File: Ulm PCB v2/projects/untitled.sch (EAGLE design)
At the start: 26 parts, among them U1 FT232RLSSOP, U2 MCP73831, U3 SPX3819-3.3, X2 USB-SMD-NS

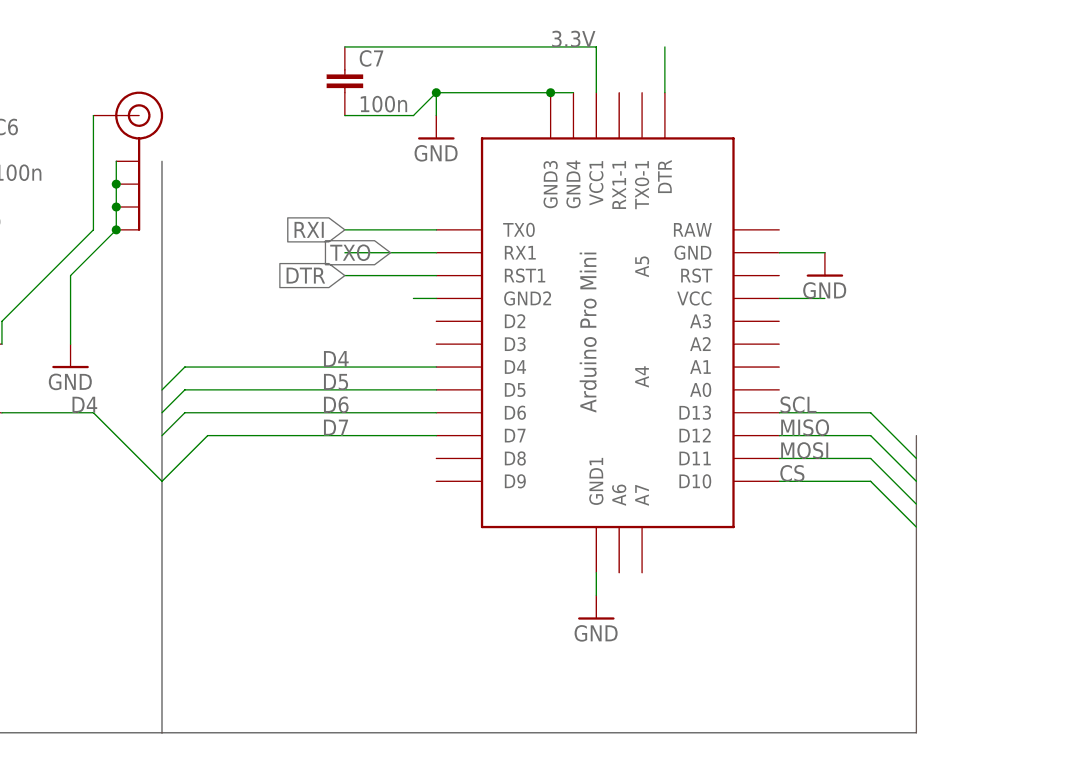
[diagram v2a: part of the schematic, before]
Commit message: nicing of some traces
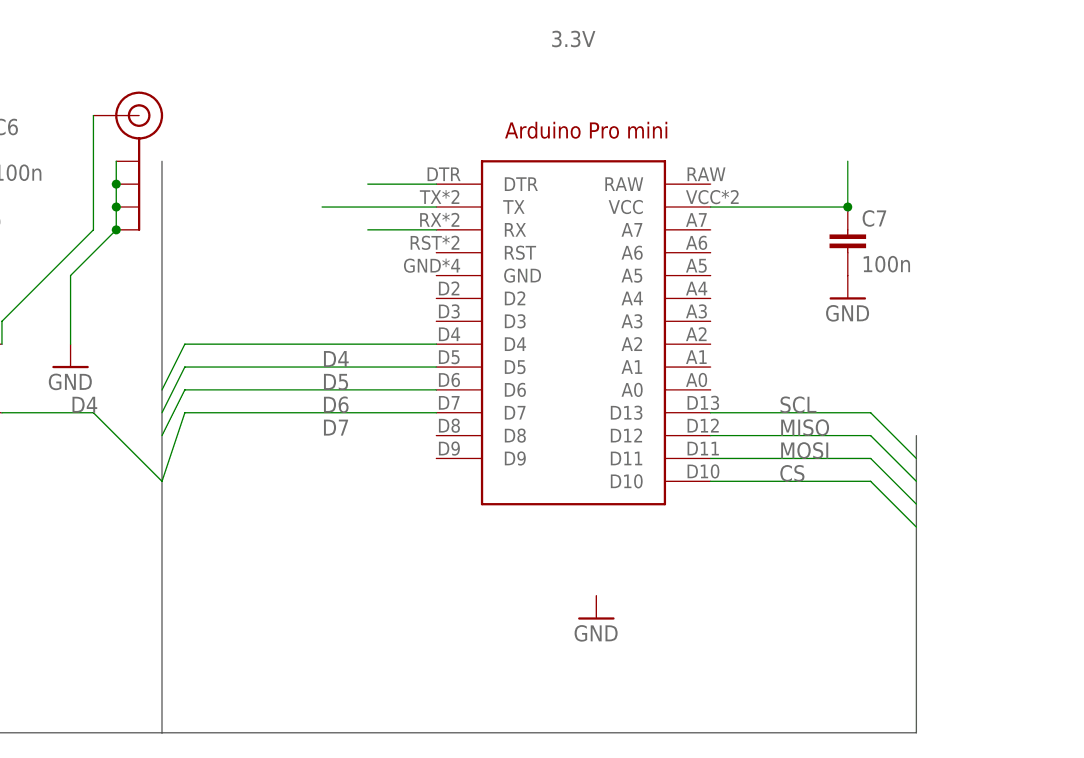
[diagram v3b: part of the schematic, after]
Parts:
- U$1: value ABK-PRO-MINI -> (none); device Arduino-clone:ABK-PRO-MINI -> arduinopromini:ARDUINO_PRO_MINI
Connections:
- removed net N$9: U$1.DTR
- net 3.3V: no longer U$1.VCC1
- net DTR: now also U$1.DTR; no longer U$1.RST1
- net GND: no longer U$1.GND, U$1.GND1, U$1.GND2, U$1.GND3, U$1.GND4
- net RXI: now also U$1.TX; no longer U$1.TX0
- net TXO: now also U$1.RX; no longer U$1.RX1
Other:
- moved on the sheet: C7
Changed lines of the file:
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@@
 </classes>
 <parts>
-<part name="U$1" library="Arduino-clone" deviceset="ABK-PRO-MINI" device=""/>
+<part name="U$1" library="arduinopromini" deviceset="ARDUINO_PRO_MINI" device=""/>
 <part name="GND4" library="supply1" deviceset="GND" device=""/>
 <part name="GND6" library="supply1" deviceset="GND" device=""/>
@@
 <part name="U$3" library="SparkFun" deviceset="5V" device=""/>
 <part name="U$4" library="SparkFun" deviceset="5V" device="" value="3.3V"/>
-<part name="GND1" library="supply1" deviceset="GND" device=""/>
 <part name="U2" library="SparkFun-PowerIC" deviceset="MCP73831" device=""/>
 <part name="R3" library="rcl" library_urn="urn:adsk.eagle:library:334" deviceset="R-EU_" device="R0603" value="330"/>
@@
 </plain>
 <instances>
-<instance part="U$1" gate="G$1" x="177.8" y="401.32"/>
-<instance part="GND4" gate="1" x="154.94" y="424.18"/>
+<instance part="U$1" gate="G$1" x="170.18" y="403.86"/>
+<instance part="GND4" gate="1" x="200.66" y="406.4"/>
 <instance part="GND6" gate="1" x="172.72" y="370.84"/>
 <instance part="C2" gate="G$1" x="-142.24" y="215.9"/>
@@
 <instance part="U$3" gate="G$1" x="-114.3" y="238.76"/>
 <instance part="U$4" gate="G$1" x="-43.18" y="233.68"/>
-<instance part="GND1" gate="1" x="198.12" y="408.94"/>
 <instance part="U2" gate="G$1" x="-86.36" y="307.34"/>
 <instance part="R3" gate="G$1" x="-106.68" y="299.72"/>
@@
 <instance part="P+3" gate="VCC" x="104.14" y="434.34"/>
 <instance part="C6" gate="G$1" x="104.14" y="424.18"/>
-<instance part="C7" gate="G$1" x="144.78" y="431.8"/>
+<instance part="C7" gate="G$1" x="200.66" y="414.02"/>
 <instance part="U$6" gate="G$1" x="93.98" y="401.32"/>
 <instance part="GND15" gate="1" x="104.14" y="416.56"/>
@@
 <net name="GND" class="0">
 <segment>
-<pinref part="U$1" gate="G$1" pin="GND4"/>
-<pinref part="U$1" gate="G$1" pin="GND3"/>
-<wire x1="170.18" y1="429.26" x2="167.64" y2="429.26" width="0.1524" layer="91"/>
-<wire x1="167.64" y1="429.26" x2="154.94" y2="429.26" width="0.1524" layer="91"/>
-<wire x1="154.94" y1="429.26" x2="154.94" y2="426.72" width="0.1524" layer="91"/>
-<junction x="167.64" y="429.26"/>
 <pinref part="GND4" gate="1" pin="GND"/>
 <pinref part="C7" gate="G$1" pin="2"/>
-<wire x1="144.78" y1="426.72" x2="152.4" y2="426.72" width="0.1524" layer="91"/>
-<wire x1="152.4" y1="426.72" x2="154.94" y2="429.26" width="0.1524" layer="91"/>
-<junction x="154.94" y="429.26"/>
-</segment>
-<segment>
-<pinref part="U$1" gate="G$1" pin="GND1"/>
-<wire x1="172.72" y1="375.92" x2="172.72" y2="373.38" width="0.1524" layer="91"/>
-<pinref part="GND6" gate="1" pin="GND"/>
-</segment>
-<segment>
-<pinref part="U$1" gate="G$1" pin="GND2"/>
-<wire x1="154.94" y1="406.4" x2="152.4" y2="406.4" width="0.1524" layer="91"/>
 </segment>
 <segment>
@@
 </segment>
 <segment>
-<pinref part="U$1" gate="G$1" pin="GND"/>
-<wire x1="193.04" y1="411.48" x2="198.12" y2="411.48" width="0.1524" layer="91"/>
-<pinref part="GND1" gate="1" pin="GND"/>
-</segment>
-<segment>
 <wire x1="-33.02" y1="279.4" x2="-33.02" y2="297.18" width="0.1524" layer="91"/>
 <pinref part="GND12" gate="1" pin="GND"/>
@@
 </segment>
 </net>
-<net name="N$9" class="0">
-<segment>
-<pinref part="U$1" gate="G$1" pin="DTR"/>
-<wire x1="180.34" y1="429.26" x2="180.34" y2="434.34" width="0.1524" layer="91"/>
-</segment>
-</net>
 <net name="USB_D-" class="0">
 <segment>
@@
 </segment>
 <segment>
-<pinref part="U$1" gate="G$1" pin="RST1"/>
-<wire x1="154.94" y1="408.94" x2="144.78" y2="408.94" width="0.1524" layer="91"/>
-<label x="144.78" y="408.94" size="1.778" layer="95" rot="R180" xref="yes"/>
+<pinref part="U$1" gate="G$1" pin="DTR"/>
+<wire x1="154.94" y1="419.1" x2="147.32" y2="419.1" width="0.1524" layer="91"/>
 </segment>
 </net>
 <net name="3.3V" class="1">
 <segment>
+<pinref part="C7" gate="G$1" pin="1"/>
+<wire x1="200.66" y1="416.56" x2="200.66" y2="421.64" width="0.1524" layer="91"/>
+<label x="167.64" y="434.34" size="1.778" layer="95"/>
 <pinref part="U$1" gate="G$1" pin="VCC"/>
-<wire x1="193.04" y1="406.4" x2="198.12" y2="406.4" width="0.1524" layer="91"/>
-</segment>
-<segment>
-<pinref part="U$1" gate="G$1" pin="VCC1"/>
-<wire x1="172.72" y1="429.26" x2="172.72" y2="434.34" width="0.1524" layer="91"/>
-<pinref part="C7" gate="G$1" pin="1"/>
-<wire x1="144.78" y1="434.34" x2="172.72" y2="434.34" width="0.1524" layer="91"/>
-<label x="167.64" y="434.34" size="1.778" layer="95"/>
+<wire x1="200.66" y1="416.56" x2="185.42" y2="416.56" width="0.1524" layer="91"/>
+<junction x="200.66" y="416.56"/>
 </segment>
 <segment>
@@
 </segment>
 <segment>
-<pinref part="U$1" gate="G$1" pin="RX1"/>
-<wire x1="154.94" y1="411.48" x2="144.78" y2="411.48" width="0.1524" layer="91"/>
-<label x="149.86" y="411.48" size="1.778" layer="95" rot="R180" xref="yes"/>
+<pinref part="U$1" gate="G$1" pin="RX"/>
+<wire x1="154.94" y1="414.02" x2="147.32" y2="414.02" width="0.1524" layer="91"/>
 </segment>
 </net>
@@
 </segment>
 <segment>
-<pinref part="U$1" gate="G$1" pin="TX0"/>
-<wire x1="154.94" y1="414.02" x2="144.78" y2="414.02" width="0.1524" layer="91"/>
-<label x="144.78" y="414.02" size="1.778" layer="95" rot="R180" xref="yes"/>
+<pinref part="U$1" gate="G$1" pin="TX"/>
+<wire x1="154.94" y1="416.56" x2="142.24" y2="416.56" width="0.1524" layer="91"/>
 </segment>
 </net>
@@
 <pinref part="U$1" gate="G$1" pin="D13"/>
 <label x="193.04" y="393.7" size="1.778" layer="95"/>
-<wire x1="193.04" y1="393.7" x2="203.2" y2="393.7" width="0.1524" layer="91"/>
+<wire x1="185.42" y1="393.7" x2="203.2" y2="393.7" width="0.1524" layer="91"/>
 <wire x1="203.2" y1="393.7" x2="208.28" y2="388.62" width="0.1524" layer="91"/>
 </segment>
@@
 <pinref part="U$1" gate="G$1" pin="D12"/>
 <label x="193.04" y="391.16" size="1.778" layer="95"/>
-<wire x1="193.04" y1="391.16" x2="203.2" y2="391.16" width="0.1524" layer="91"/>
+<wire x1="185.42" y1="391.16" x2="203.2" y2="391.16" width="0.1524" layer="91"/>
 <wire x1="203.2" y1="391.16" x2="208.28" y2="386.08" width="0.1524" layer="91"/>
 </segment>
@@
 <pinref part="U$1" gate="G$1" pin="D11"/>
 <label x="193.04" y="388.62" size="1.778" layer="95"/>
-<wire x1="193.04" y1="388.62" x2="203.2" y2="388.62" width="0.1524" layer="91"/>
+<wire x1="185.42" y1="388.62" x2="203.2" y2="388.62" width="0.1524" layer="91"/>
 <wire x1="203.2" y1="388.62" x2="208.28" y2="383.54" width="0.1524" layer="91"/>
 </segment>
@@
 <pinref part="U$1" gate="G$1" pin="D10"/>
 <label x="193.04" y="386.08" size="1.778" layer="95"/>
-<wire x1="193.04" y1="386.08" x2="203.2" y2="386.08" width="0.1524" layer="91"/>
+<wire x1="185.42" y1="386.08" x2="203.2" y2="386.08" width="0.1524" layer="91"/>
 <wire x1="203.2" y1="386.08" x2="208.28" y2="381" width="0.1524" layer="91"/>
 </segment>
@@
 <pinref part="U$1" gate="G$1" pin="D7"/>
 <label x="142.24" y="391.16" size="1.778" layer="95"/>
-<wire x1="154.94" y1="391.16" x2="129.54" y2="391.16" width="0.1524" layer="91"/>
-<wire x1="129.54" y1="391.16" x2="124.46" y2="386.08" width="0.1524" layer="91"/>
+<wire x1="154.94" y1="393.7" x2="127" y2="393.7" width="0.1524" layer="91"/>
+<wire x1="127" y1="393.7" x2="124.46" y2="386.08" width="0.1524" layer="91"/>
 </segment>
 </net>
@@
 <pinref part="U$1" gate="G$1" pin="D5"/>
 <label x="142.24" y="396.24" size="1.778" layer="95"/>
-<wire x1="154.94" y1="396.24" x2="127" y2="396.24" width="0.1524" layer="91"/>
-<wire x1="127" y1="396.24" x2="124.46" y2="393.7" width="0.1524" layer="91"/>
+<wire x1="154.94" y1="398.78" x2="127" y2="398.78" width="0.1524" layer="91"/>
+<wire x1="127" y1="398.78" x2="124.46" y2="393.7" width="0.1524" layer="91"/>
 </segment>
 </net>
@@
 <pinref part="U$1" gate="G$1" pin="D4"/>
 <label x="142.24" y="398.78" size="1.778" layer="95"/>
-<wire x1="154.94" y1="398.78" x2="127" y2="398.78" width="0.1524" layer="91"/>
-<wire x1="127" y1="398.78" x2="124.46" y2="396.24" width="0.1524" layer="91"/>
+<wire x1="154.94" y1="401.32" x2="127" y2="401.32" width="0.1524" layer="91"/>
+<wire x1="127" y1="401.32" x2="124.46" y2="396.24" width="0.1524" layer="91"/>
 </segment>
 <segment>
@@
 <pinref part="U$1" gate="G$1" pin="D6"/>
 <label x="142.24" y="393.7" size="1.778" layer="95"/>
-<wire x1="154.94" y1="393.7" x2="127" y2="393.7" width="0.1524" layer="91"/>
-<wire x1="127" y1="393.7" x2="124.46" y2="391.16" width="0.1524" layer="91"/>
-</segment>
-<segment>
+<wire x1="154.94" y1="396.24" x2="127" y2="396.24" width="0.1524" layer="91"/>
+<wire x1="127" y1="396.24" x2="124.46" y2="391.16" width="0.1524" layer="91"/>
+</segment>
+<segment>

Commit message: replaced some of the 0603 Resistors with 0805
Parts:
- R-PROG2, R1, R2, R3: device rcl:R-EU_R0603 -> rcl:R-EU_R0805
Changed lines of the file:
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@@
 <?xml version="1.0" encoding="utf-8"?>
 <!DOCTYPE eagle SYSTEM "eagle.dtd">
-<eagle version="8.2.2">
+<eagle version="8.3.1">
 <drawing>
 <settings>
 <setting alwaysvectorfont="no"/>
+<setting keepoldvectorfont="yes"/>
 <setting verticaltext="up"/>
 </settings>
@@
 <part name="GND7" library="SparkFun" deviceset="GND" device=""/>
 <part name="GND8" library="SparkFun" deviceset="GND" device=""/>
-<part name="R1" library="rcl" library_urn="urn:adsk.eagle:library:334" deviceset="R-EU_" device="R0603" value="1K"/>
-<part name="R2" library="rcl" library_urn="urn:adsk.eagle:library:334" deviceset="R-EU_" device="R0603" value="1K"/>
+<part name="R1" library="rcl" library_urn="urn:adsk.eagle:library:334" deviceset="R-EU_" device="R0805" package3d_urn="urn:adsk.eagle:package:23553/2" value="1K"/>
+<part name="R2" library="rcl" library_urn="urn:adsk.eagle:library:334" deviceset="R-EU_" device="R0805" package3d_urn="urn:adsk.eagle:package:23553/2" value="1K"/>
 <part name="LED1" library="SparkFun" deviceset="LED" device="0603" value="Red"/>
 <part name="LED2" library="SparkFun" deviceset="LED" device="0603" value="Green"/>
@@
 <part name="U$4" library="SparkFun" deviceset="5V" device="" value="3.3V"/>
 <part name="U2" library="SparkFun-PowerIC" deviceset="MCP73831" device=""/>
-<part name="R3" library="rcl" library_urn="urn:adsk.eagle:library:334" deviceset="R-EU_" device="R0603" value="330"/>
+<part name="R3" library="rcl" library_urn="urn:adsk.eagle:library:334" deviceset="R-EU_" device="R0805" package3d_urn="urn:adsk.eagle:package:23553/2" value="330"/>
 <part name="C4" library="rcl" library_urn="urn:adsk.eagle:library:334" deviceset="C-EU" device="C0805" value="10u"/>
 <part name="GND12" library="SparkFun" deviceset="GND" device=""/>
-<part name="R-PROG2" library="rcl" library_urn="urn:adsk.eagle:library:334" deviceset="R-EU_" device="R0603" value="10k"/>
+<part name="R-PROG2" library="rcl" library_urn="urn:adsk.eagle:library:334" deviceset="R-EU_" device="R0805" package3d_urn="urn:adsk.eagle:package:23553/2" value="10k"/>
 <part name="GND14" library="SparkFun" deviceset="GND" device=""/>
 <part name="FRAME1" library="frames" deviceset="A3L-LOC" device=""/>
@@
 </sheet>
 </sheets>
+<errors>
+</errors>
 </schematic>
 </drawing>
 <compatibility>
 <note version="8.2" severity="warning">
-Since Version 8.2, Eagle supports online libraries. The ids
+Since Version 8.2, EAGLE supports online libraries. The ids
 of those online libraries will not be understood (or retained)
 with this version.
 </note>
+<note version="8.3" severity="warning">
+Since Version 8.3, EAGLE supports URNs for individual library
+assets (packages, symbols, and devices). The URNs of those assets
+will not be understood (or retained) with this version.
+</note>
+<note version="8.3" severity="warning">
+Since Version 8.3, EAGLE supports the association of 3D packages
+with devices in libraries, schematics, and board files. Those 3D
+packages will not be understood (or retained) with this version.
+</note>
 </compatibility>
